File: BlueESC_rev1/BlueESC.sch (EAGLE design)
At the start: 75 parts, among them J1 AVR_SPI_PRG_6PTH, Q1 BC817-40W, Q2 BC817-40W, Q3 BC817-40W, Q4 SI7370, Q5 SI7370, Q6 SiR158DP, Q7 SI7370, Q8 SI7370, Q9 SI7370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

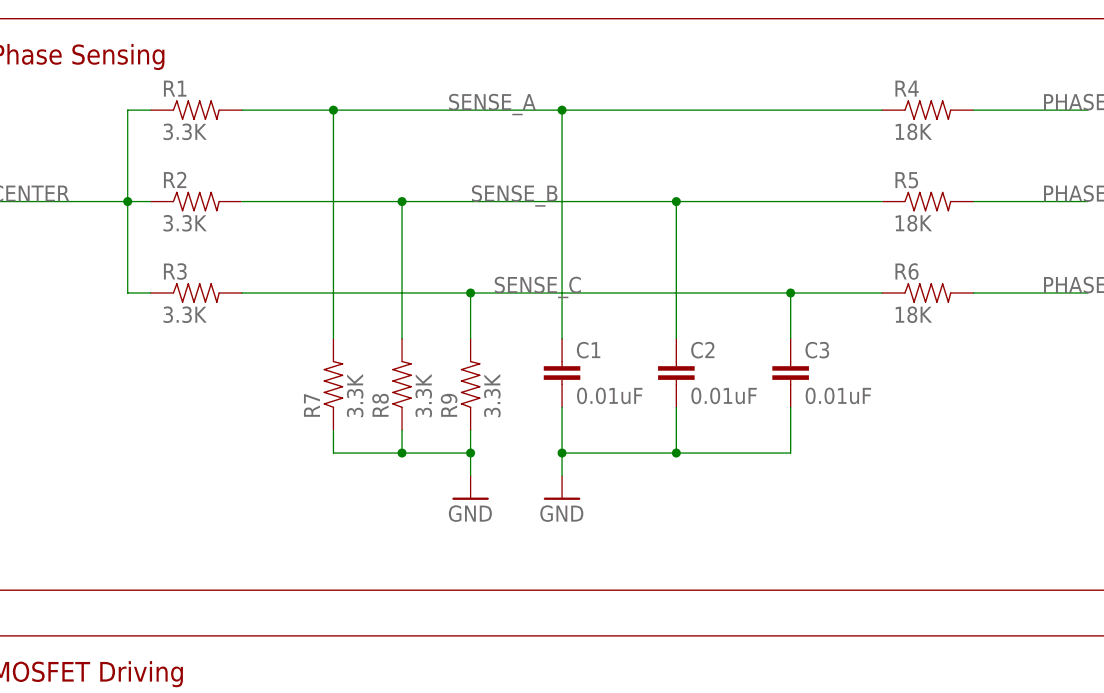
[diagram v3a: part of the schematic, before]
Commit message: Removed sense filtering capacitors and changed voltage divider resistor values.
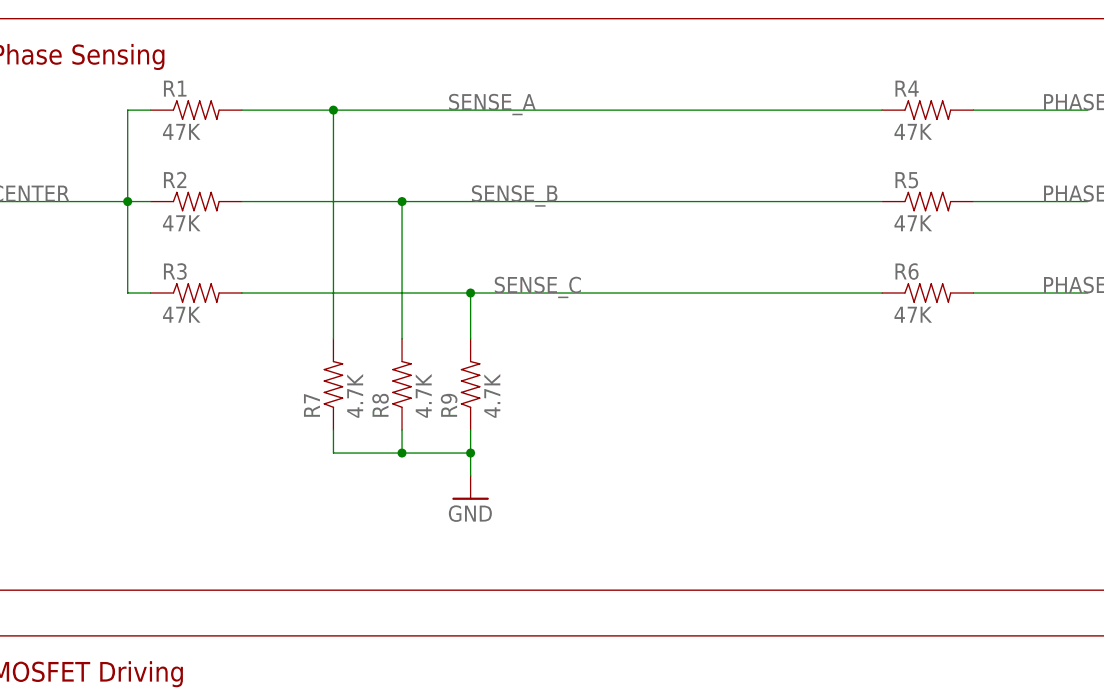
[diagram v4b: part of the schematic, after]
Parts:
- removed C1, C2, C3: 0.01uF, SparkFun-Capacitors:CAP0603-CAP
- R1, R2, R3: value 3.3K -> 47K
- R4, R5, R6: value 18K -> 47K
- R7, R8, R9: value 3.3K -> 4.7K
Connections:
- net GND: no longer C1.2, C2.2, C3.2
- net SENSE_A: no longer C1.1
- net SENSE_B: no longer C2.1
- net SENSE_C: no longer C3.1
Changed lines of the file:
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@@
 <parts>
 <part name="U1" library="SparkFun-DigitalIC" deviceset="ATMEGA168" device="" value="ATMEGA168"/>
-<part name="R1" library="SparkFun-Resistors" deviceset="33KOHM1/10W1%(0603)" device="" value="3.3K"/>
-<part name="R2" library="SparkFun-Resistors" deviceset="33KOHM1/10W1%(0603)" device="" value="3.3K"/>
-<part name="R3" library="SparkFun-Resistors" deviceset="33KOHM1/10W1%(0603)" device="" value="3.3K"/>
-<part name="R4" library="SparkFun-Resistors" deviceset="33KOHM1/10W1%(0603)" device="" value="18K"/>
-<part name="R5" library="SparkFun-Resistors" deviceset="33KOHM1/10W1%(0603)" device="" value="18K"/>
-<part name="R6" library="SparkFun-Resistors" deviceset="33KOHM1/10W1%(0603)" device="" value="18K"/>
-<part name="R7" library="SparkFun-Resistors" deviceset="RESISTOR" device="0603" value="3.3K"/>
-<part name="R8" library="SparkFun-Resistors" deviceset="RESISTOR" device="0603" value="3.3K"/>
-<part name="R9" library="SparkFun-Resistors" deviceset="RESISTOR" device="0603" value="3.3K"/>
-<part name="C1" library="SparkFun-Capacitors" deviceset="CAP" device="0603-CAP" value="0.01uF"/>
-<part name="C2" library="SparkFun-Capacitors" deviceset="CAP" device="0603-CAP" value="0.01uF"/>
-<part name="C3" library="SparkFun-Capacitors" deviceset="CAP" device="0603-CAP" value="0.01uF"/>
+<part name="R1" library="SparkFun-Resistors" deviceset="33KOHM1/10W1%(0603)" device="" value="47K"/>
+<part name="R2" library="SparkFun-Resistors" deviceset="33KOHM1/10W1%(0603)" device="" value="47K"/>
+<part name="R3" library="SparkFun-Resistors" deviceset="33KOHM1/10W1%(0603)" device="" value="47K"/>
+<part name="R4" library="SparkFun-Resistors" deviceset="33KOHM1/10W1%(0603)" device="" value="47K"/>
+<part name="R5" library="SparkFun-Resistors" deviceset="33KOHM1/10W1%(0603)" device="" value="47K"/>
+<part name="R6" library="SparkFun-Resistors" deviceset="33KOHM1/10W1%(0603)" device="" value="47K"/>
+<part name="R7" library="SparkFun-Resistors" deviceset="RESISTOR" device="0603" value="4.7K"/>
+<part name="R8" library="SparkFun-Resistors" deviceset="RESISTOR" device="0603" value="4.7K"/>
+<part name="R9" library="SparkFun-Resistors" deviceset="RESISTOR" device="0603" value="4.7K"/>
 <part name="GND1" library="SparkFun-Aesthetics" deviceset="GND" device=""/>
-<part name="GND2" library="SparkFun-Aesthetics" deviceset="GND" device=""/>
 <part name="R10" library="SparkFun-Resistors" deviceset="33KOHM1/10W1%(0603)" device="" value="10K"/>
 <part name="R11" library="SparkFun-Resistors" deviceset="33KOHM1/10W1%(0603)" device="" value="1K"/>
@@
 <instance part="R8" gate="G$1" x="256.54" y="154.94" rot="R90"/>
 <instance part="R9" gate="G$1" x="264.16" y="154.94" rot="R90"/>
-<instance part="C1" gate="G$1" x="274.32" y="154.94"/>
-<instance part="C2" gate="G$1" x="287.02" y="154.94"/>
-<instance part="C3" gate="G$1" x="299.72" y="154.94"/>
 <instance part="GND1" gate="1" x="264.16" y="142.24"/>
-<instance part="GND2" gate="1" x="274.32" y="142.24"/>
 <instance part="R10" gate="G$1" x="2.54" y="96.52" rot="R90"/>
 <instance part="R11" gate="G$1" x="2.54" y="78.74" rot="R90"/>
@@
 <wire x1="238.76" y1="185.42" x2="248.92" y2="185.42" width="0.1524" layer="91"/>
 <pinref part="R7" gate="G$1" pin="2"/>
-<wire x1="248.92" y1="185.42" x2="274.32" y2="185.42" width="0.1524" layer="91"/>
-<wire x1="274.32" y1="185.42" x2="309.88" y2="185.42" width="0.1524" layer="91"/>
+<wire x1="248.92" y1="185.42" x2="309.88" y2="185.42" width="0.1524" layer="91"/>
 <wire x1="248.92" y1="160.02" x2="248.92" y2="185.42" width="0.1524" layer="91"/>
 <junction x="248.92" y="185.42"/>
-<pinref part="C1" gate="G$1" pin="1"/>
-<wire x1="274.32" y1="160.02" x2="274.32" y2="185.42" width="0.1524" layer="91"/>
-<junction x="274.32" y="185.42"/>
 <label x="261.62" y="185.42" size="1.778" layer="95"/>
 </segment>
@@
 <wire x1="238.76" y1="175.26" x2="256.54" y2="175.26" width="0.1524" layer="91"/>
 <pinref part="R8" gate="G$1" pin="2"/>
-<wire x1="256.54" y1="175.26" x2="287.02" y2="175.26" width="0.1524" layer="91"/>
-<wire x1="287.02" y1="175.26" x2="309.88" y2="175.26" width="0.1524" layer="91"/>
+<wire x1="256.54" y1="175.26" x2="309.88" y2="175.26" width="0.1524" layer="91"/>
 <wire x1="256.54" y1="160.02" x2="256.54" y2="175.26" width="0.1524" layer="91"/>
 <junction x="256.54" y="175.26"/>
-<pinref part="C2" gate="G$1" pin="1"/>
-<wire x1="287.02" y1="160.02" x2="287.02" y2="175.26" width="0.1524" layer="91"/>
-<junction x="287.02" y="175.26"/>
 <label x="264.16" y="175.26" size="1.778" layer="95"/>
 </segment>
@@
 <wire x1="238.76" y1="165.1" x2="264.16" y2="165.1" width="0.1524" layer="91"/>
 <pinref part="R9" gate="G$1" pin="2"/>
-<wire x1="264.16" y1="165.1" x2="299.72" y2="165.1" width="0.1524" layer="91"/>
-<wire x1="299.72" y1="165.1" x2="309.88" y2="165.1" width="0.1524" layer="91"/>
+<wire x1="264.16" y1="165.1" x2="309.88" y2="165.1" width="0.1524" layer="91"/>
 <wire x1="264.16" y1="160.02" x2="264.16" y2="165.1" width="0.1524" layer="91"/>
 <junction x="264.16" y="165.1"/>
-<pinref part="C3" gate="G$1" pin="1"/>
-<wire x1="299.72" y1="160.02" x2="299.72" y2="165.1" width="0.1524" layer="91"/>
-<junction x="299.72" y="165.1"/>
 <label x="266.7" y="165.1" size="1.778" layer="95"/>
 </segment>
@@
 </segment>
 <segment>
-<pinref part="C1" gate="G$1" pin="2"/>
-<pinref part="GND2" gate="1" pin="GND"/>
-<wire x1="274.32" y1="152.4" x2="274.32" y2="147.32" width="0.1524" layer="91"/>
-<pinref part="C3" gate="G$1" pin="2"/>
-<wire x1="274.32" y1="147.32" x2="274.32" y2="144.78" width="0.1524" layer="91"/>
-<wire x1="299.72" y1="152.4" x2="299.72" y2="147.32" width="0.1524" layer="91"/>
-<wire x1="299.72" y1="147.32" x2="287.02" y2="147.32" width="0.1524" layer="91"/>
-<junction x="274.32" y="147.32"/>
-<pinref part="C2" gate="G$1" pin="2"/>
-<wire x1="287.02" y1="147.32" x2="274.32" y2="147.32" width="0.1524" layer="91"/>
-<wire x1="287.02" y1="152.4" x2="287.02" y2="147.32" width="0.1524" layer="91"/>
-<junction x="287.02" y="147.32"/>
-</segment>
-<segment>
